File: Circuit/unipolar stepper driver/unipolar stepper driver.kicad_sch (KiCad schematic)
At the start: 20 parts, among them Q1 S8050, Q2 S8050, Q3 S8050, Q4 S8050

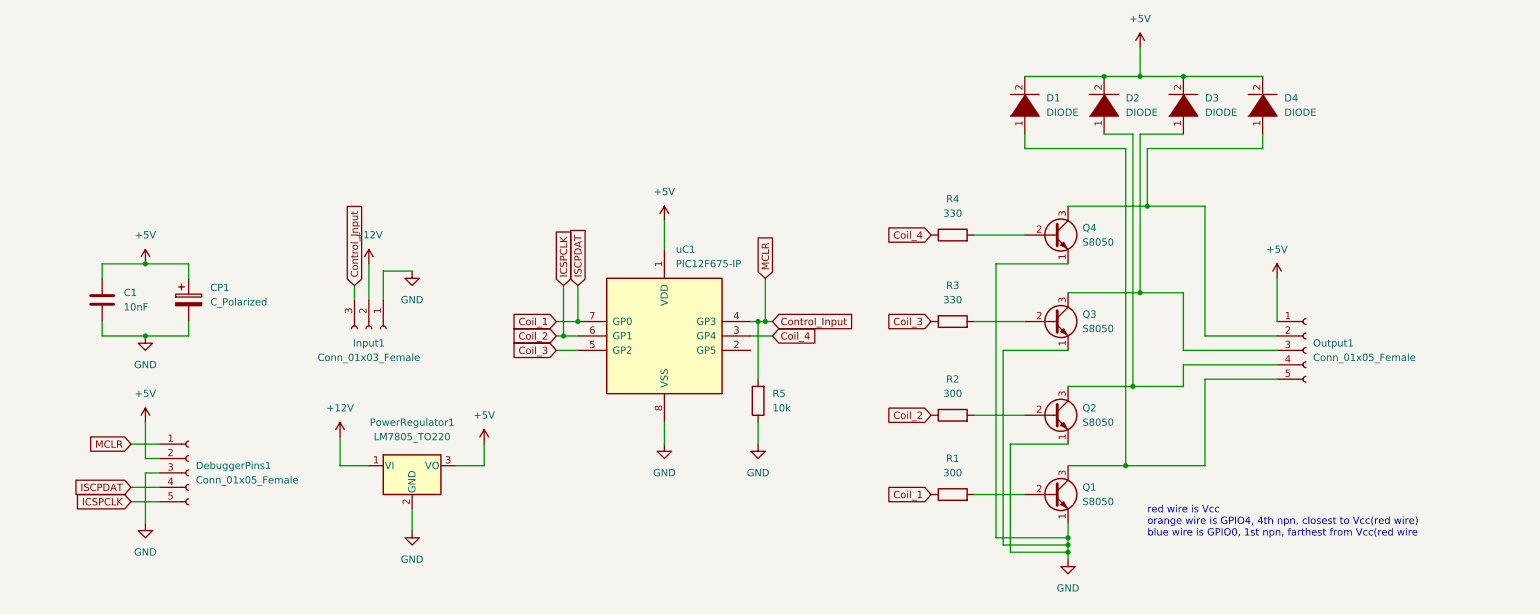
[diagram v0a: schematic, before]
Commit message: unipolar circuit development
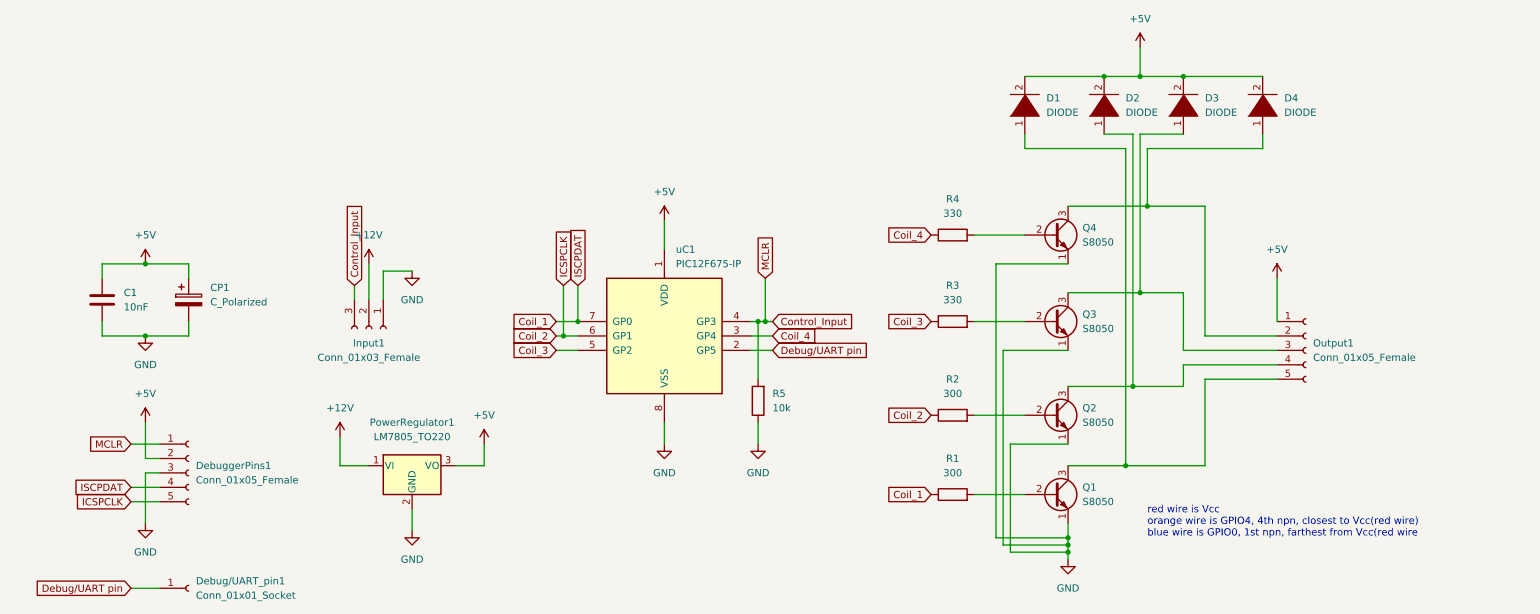
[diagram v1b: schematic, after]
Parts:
- added Debug/UART_pin1: Conn_01x01_Socket, Connector_PinSocket_2.54mm:PinSocket_1x01_P2.54mm_Vertical, symbol Connector:Conn_01x01_Socket
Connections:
- net Debug/UART pin: now reaches uC1.2 (GP5)
- net Debug/UART pin: now also Debug/UART_pin1.1 (Pin_1)
